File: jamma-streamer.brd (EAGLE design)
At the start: 180.3 x 92 mm, 44 parts, among them IC1 LM7805, J1 Audio line out, J2 ICSP, J3 SDCARD, J4 292304-1, U1 CD74HC165MD16-M, U2 ATMEGA328PB-AUR, U3 74HC4050D, U4 TLV757X / LP298X, U5 CD74HC165MD16-M, U6 CD74HC165MD16-M, U7 FT232RL, Y1 16MHz

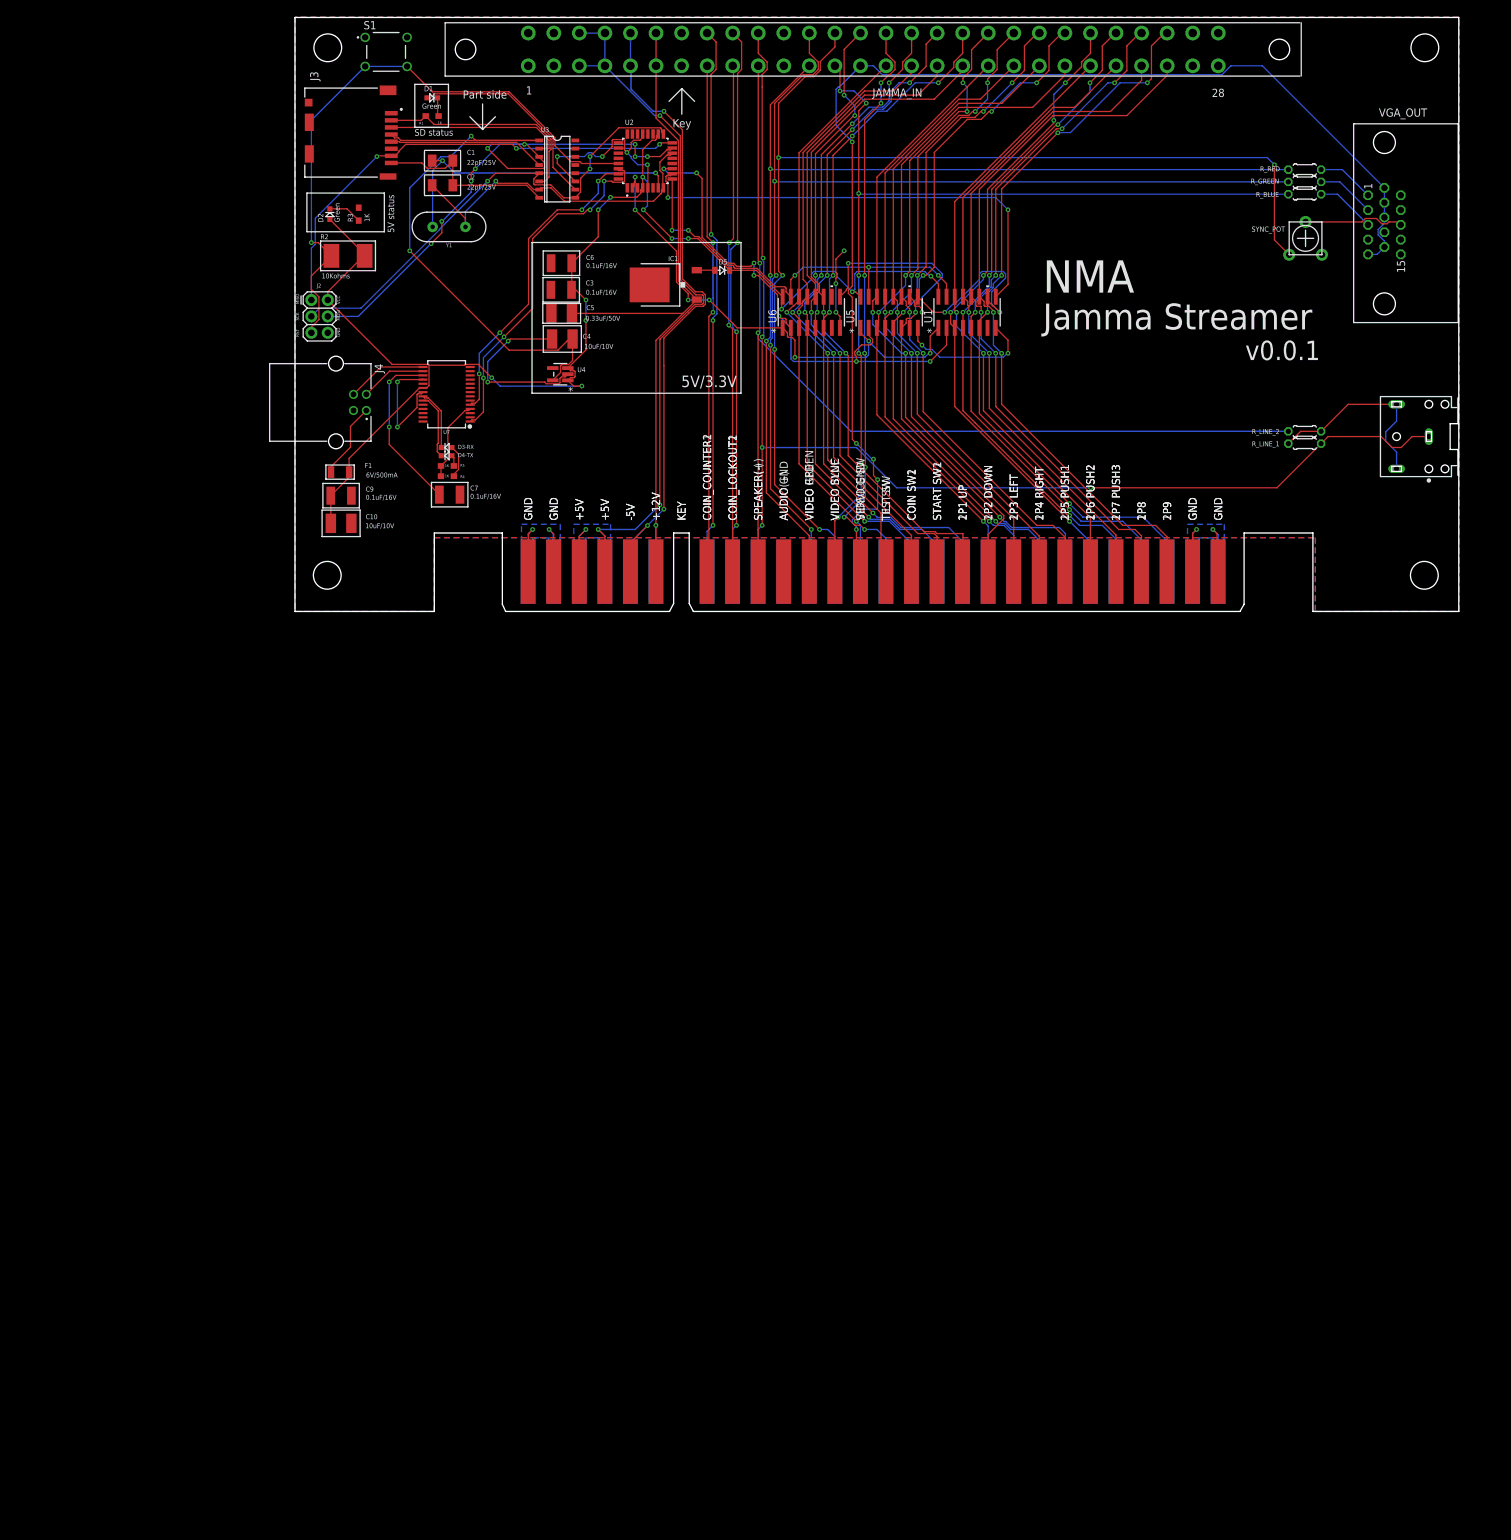
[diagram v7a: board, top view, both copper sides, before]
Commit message: Better routes (unfinished) and audio circuit
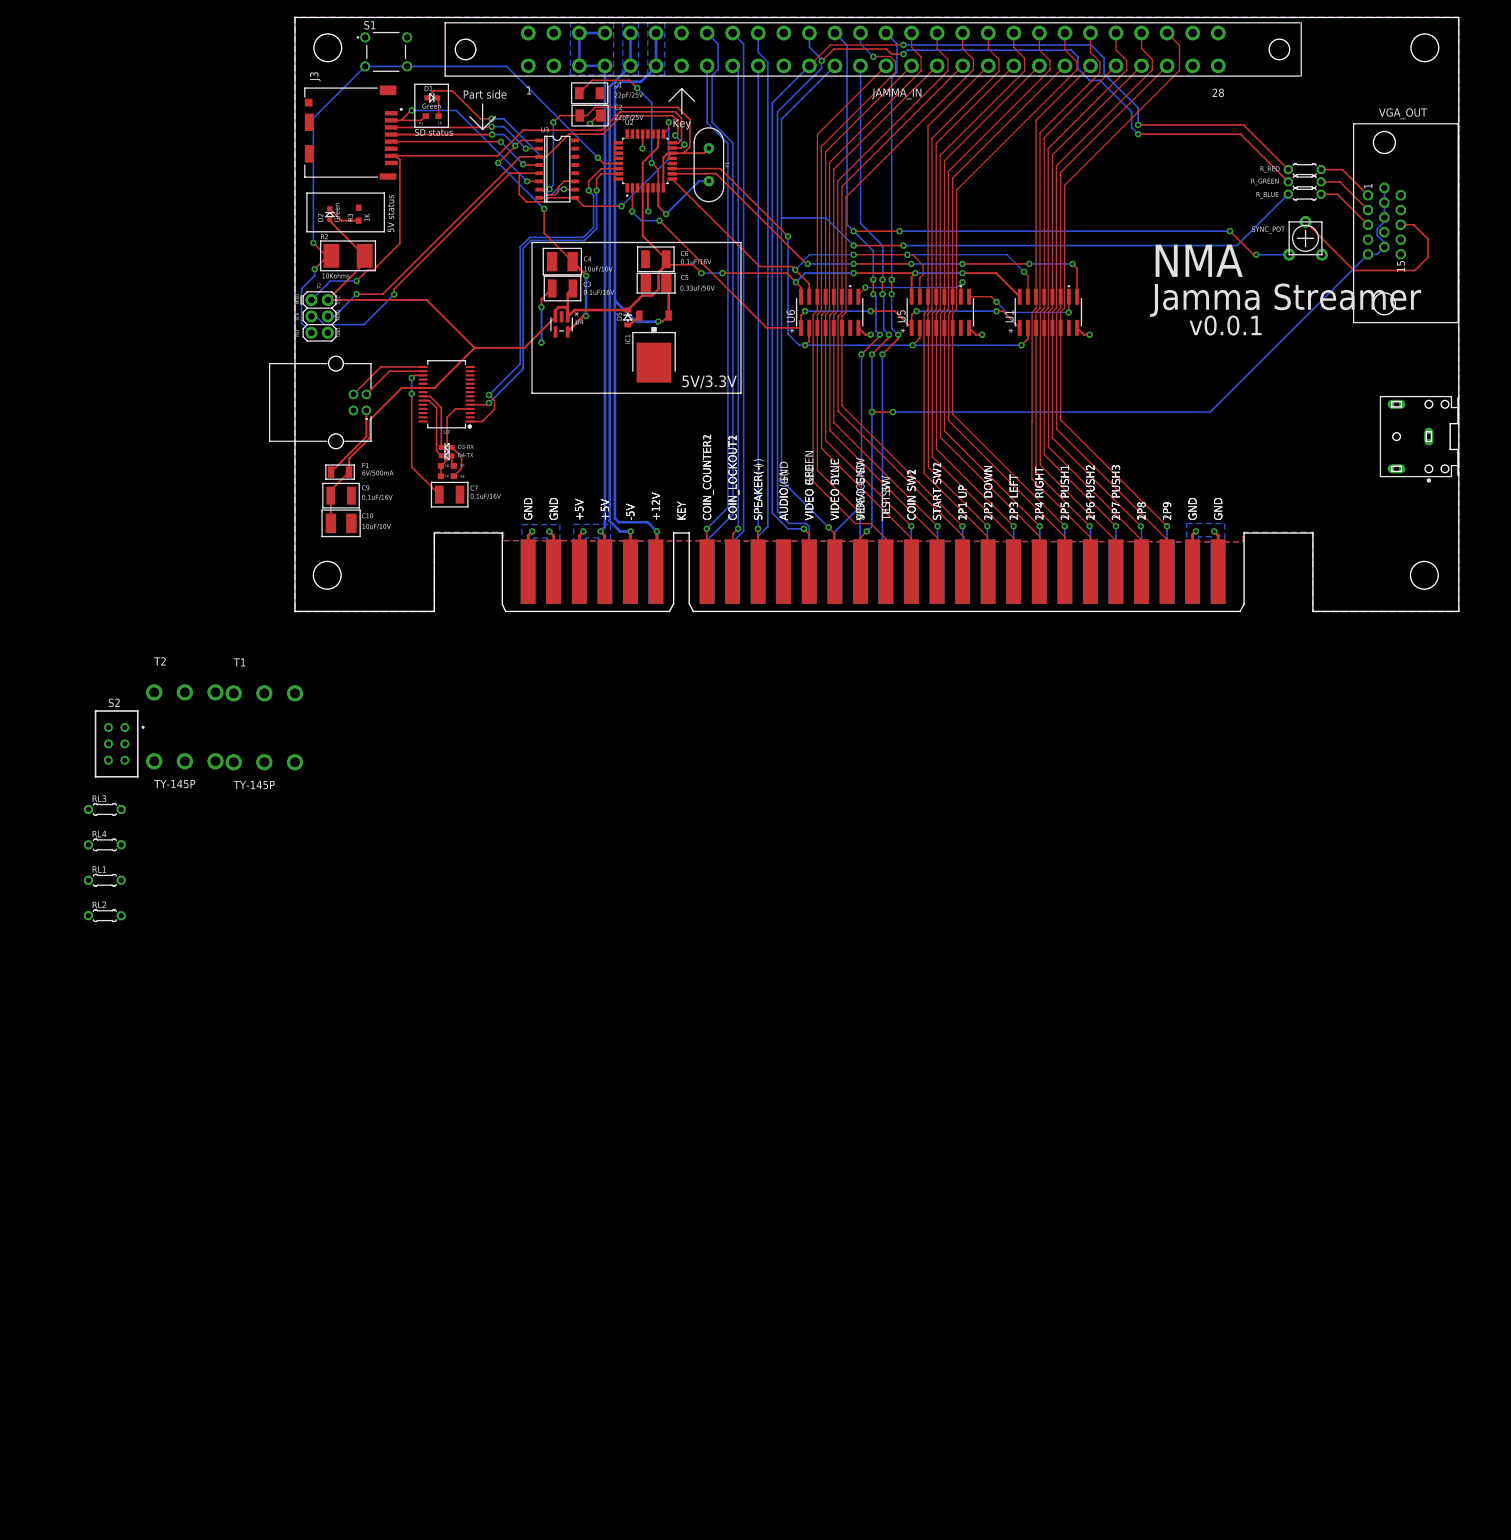
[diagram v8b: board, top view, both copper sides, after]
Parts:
- removed R_LINE_1: 1K, rcl:0204/5
- removed R_LINE_2: 10K, rcl:0204/5
- added RL1, RL3: 10K, rcl:0204/5
- added RL2, RL4: 1K, rcl:0204/5
- added S2: SS22SDP2, SamacSys_Parts:SS22SDP2(DPDT)
- added T1, T2: TY-145P, TRIAD-TY-145P:TRIAD-TY-145P
- J4: value 292304-1 -> USB
- moved Y1 41.4 mm to (64.1, 69.2), turned to 270 degrees
- moved C2 25.3 mm to (45.7, 76.8)
- moved C1 25.1 mm to (45.7, 80.3)
- moved D5 16.4 mm to (51.6, 45.5), turned to 270 degrees
- moved C5 15.4 mm to (56.0, 50.9)
- moved C6 14.6 mm to (55.9, 54.6)
- moved U1 12.6 mm to (116.7, 46.4)
- moved C4 12.0 mm to (41.4, 54.2)
- moved IC1 9.72 mm to (55.6, 41.1), turned to 180 degrees
- moved U5 7.92 mm to (100.0, 46.4)
- moved U4 7.72 mm to (41.3, 44.5), turned to 270 degrees
- moved U6 2.84 mm to (82.9, 46.4)
- moved C3 0.29 mm to (41.5, 50.0)
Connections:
- new net N$24: RL1.2, RL4.1, T1.1
- new net N$25: RL2.2, RL4.2, S2.5, T1.3, T2.3
- new net N$26: J1.2, T1.4
- new net N$28: RL2.1, RL3.2, T2.1
- new net N$30: J1.3, T2.4
- net GND: now also J1.1, S2.6, T1.6, T2.6
- net N$4: now also RL3.1, S2.2; no longer J1.2, J1.3, R_LINE_1.1, R_LINE_2.2
- net SPK+: now also RL1.1, S2.1; no longer R_LINE_2.1
- net SPK-: now also S2.3, S2.4; no longer J1.1, R_LINE_1.2
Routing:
- net GND: track 196.4 -> 83.3 mm, vias 17 -> 12
- net SPK-: track 195.4 -> 84.8 mm, vias 5 -> 0
- net SPK+: track 167.6 -> 78.4 mm, vias 2 -> 1
- net VCC_2: track 97.2 -> 60.9 mm, vias 2 -> 6
- net N$4: track 30.7 -> 0.00 mm
- net P: track 185.4 -> 158.4 mm, vias 5 -> 8
- net 26: track 112.5 -> 92.6 mm, vias 2 -> 0
- net JAMMA+5V: track 130.9 -> 111.4 mm, vias 4 -> 2
- net BLUE: track 150.6 -> 168.8 mm, vias 7 -> 3
- net _D: track 116.9 -> 98.7 mm, vias 5 -> 1
- net 25: track 107.3 -> 90.3 mm, vias 2 -> 0
- net DI: track 90.9 -> 74.0 mm, vias 9 -> 3
- net N$3: track 15.6 -> 30.9 mm
- net 22: track 107.5 -> 93.3 mm, vias 2 -> 0
- net _C: track 110.4 -> 96.3 mm, vias 5 -> 1
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- added copper zone on layer 16, net JAMMA+12
- added copper zone on layer 16, net JAMMA+5
- added copper zone on layer 16, net JAMMA-5
